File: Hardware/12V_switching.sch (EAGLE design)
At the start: 10 parts, among them IC5 LM2576D2TR4-5G, J1 POWERPOLE_POWER45A, J2 POWERPOLE_POWER45A

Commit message: Fix switching regulator reference
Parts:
- IC5: value LM2576D2TR4-5G -> LM2576D2TR4-012G; device LM2576D2TR4-5G:LM2576D2TR4-5G -> LM2576:LM2576D2TR4-012G
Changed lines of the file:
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@@
 </classes>
 <parts>
-<part name="IC5" library="LM2576D2TR4-5G" deviceset="LM2576D2TR4-5G" device=""/>
+<part name="IC5" library="LM2576" deviceset="LM2576D2TR4-012G" device=""/>
 <part name="GND12" library="supply1" deviceset="GND" device=""/>
 <part name="D2" library="diode" deviceset="DIODE-" device="DO-214AC" value="SAC32"/>

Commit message: Fix dimention layer on  RTI-Dome-eth.brd, added MPN on all component for mouser.
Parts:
- removed X11: (no value), con-ptr500:AK500/2
- added J3: POWERPOLE_POWER45A, powerpoles:POWERPOLE_POWER45A
- U$1: device rti:C-EU'1206' -> rti:C-EU'0805'
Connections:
- net +VIN: no longer X11-1.KL
- net GND: no longer X11-2.KL
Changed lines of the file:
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@@
 <part name="C10" library="rcl" deviceset="CPOL-EU" device="UD-10X10" value="100uF"/>
 <part name="C11" library="rcl" deviceset="CPOL-EU" device="UD-10X10" value="1000uF"/>
-<part name="U$1" library="rti" deviceset="C-EU" device="'1206'" value="47uF"/>
+<part name="U$1" library="rti" deviceset="C-EU" device="'0805'" value="47uF"/>
 <part name="U$2" library="rti" deviceset="C-EU" device="'1206'" value="47uF"/>
 <part name="J1" library="powerpoles" deviceset="POWERPOLE_POWER" device="45A"/>
 <part name="J2" library="powerpoles" deviceset="POWERPOLE_POWER" device="45A"/>
-<part name="X11" library="con-ptr500" deviceset="AK500/2" device=""/>
+<part name="J3" library="powerpoles" deviceset="POWERPOLE_POWER" device="45A"/>
 </parts>
 <sheets>
@@
 <instance part="J1" gate="G$1" x="10.16" y="48.26" rot="R180"/>
 <instance part="J2" gate="G$1" x="157.48" y="30.48"/>
-<instance part="X11" gate="-1" x="15.24" y="12.7"/>
-<instance part="X11" gate="-2" x="15.24" y="7.62"/>
+<instance part="J3" gate="G$1" x="172.72" y="5.08"/>
 </instances>
 <busses>
@@
 </segment>
 <segment>
-<wire x1="22.86" y1="7.62" x2="20.32" y2="7.62" width="0.1524" layer="91"/>
-<label x="22.86" y="7.62" size="1.016" layer="95" rot="MR180" xref="yes"/>
-<pinref part="X11" gate="-2" pin="KL"/>
+<wire x1="160.02" y1="0" x2="162.56" y2="0" width="0.1524" layer="91"/>
+<label x="160.02" y="0" size="1.016" layer="95" rot="MR0" xref="yes"/>
 </segment>
 </net>
@@
 </segment>
 <segment>
-<wire x1="22.86" y1="12.7" x2="20.32" y2="12.7" width="0.1524" layer="91"/>
-<label x="22.86" y="12.7" size="1.016" layer="95" rot="MR180" xref="yes"/>
-<pinref part="X11" gate="-1" pin="KL"/>
+<wire x1="160.02" y1="10.16" x2="162.56" y2="10.16" width="0.1524" layer="91"/>
+<label x="160.02" y="10.16" size="1.016" layer="95" rot="MR0" xref="yes"/>
 </segment>
 </net>

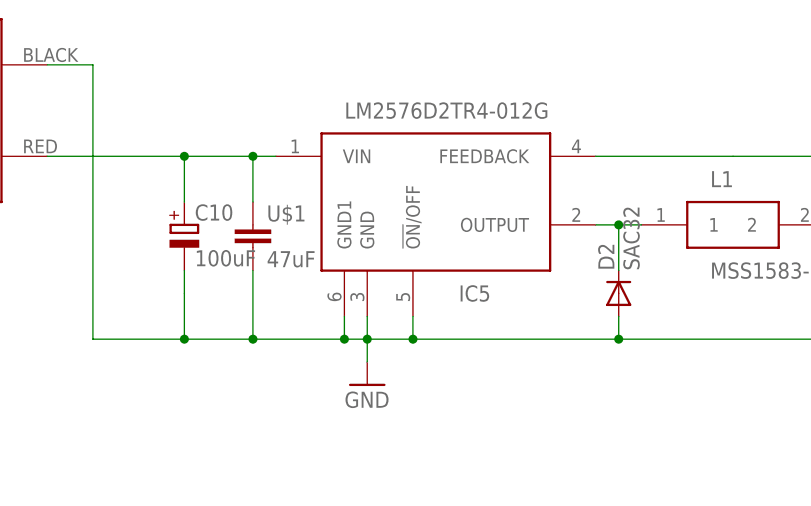
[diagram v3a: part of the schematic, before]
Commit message: Change pin mode for better interrupt detection
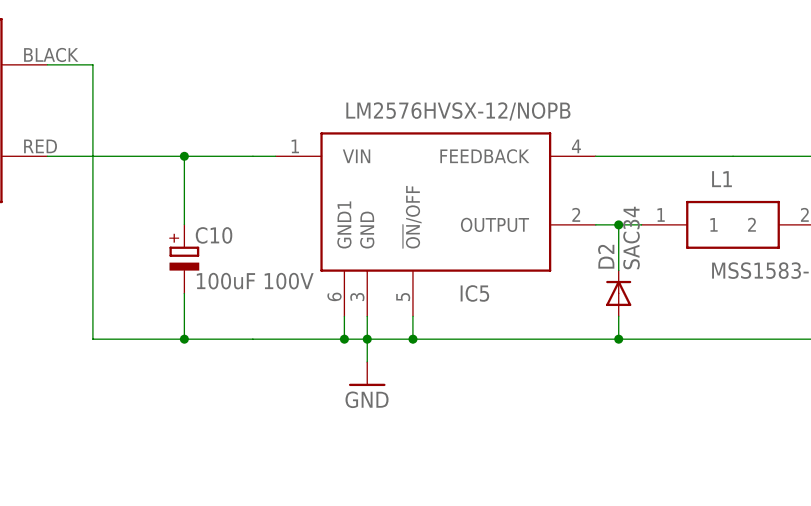
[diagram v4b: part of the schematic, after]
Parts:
- removed U$1: 47uF, rti:C-EU'0805'
- C10: value 100uF -> 100uF 100V
- D2: value SAC32 -> SAC34
- IC5: value LM2576D2TR4-012G -> LM2576HVSX-12/NOPB; MOUSER_PART_NUMBER (none) -> LM2576HVSX-12/NOPB; MPN (none) -> LM2576HVSX-12/NOPB
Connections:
- net +VIN: no longer U$1.1
- net GND: no longer U$1.2
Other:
- moved on the sheet: C10
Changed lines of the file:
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@@
 </classes>
 <parts>
-<part name="IC5" library="LM2576" deviceset="LM2576D2TR4-012G" device=""/>
+<part name="IC5" library="LM2576" deviceset="LM2576D2TR4-012G" device="" value="LM2576HVSX-12/NOPB">
+<attribute name="MOUSER_PART_NUMBER" value=" LM2576HVSX-12/NOPB"/>
+<attribute name="MPN" value=" LM2576HVSX-12/NOPB"/>
+</part>
 <part name="GND12" library="supply1" deviceset="GND" device=""/>
-<part name="D2" library="diode" deviceset="DIODE-" device="DO-214AC" value="SAC32"/>
+<part name="D2" library="diode" deviceset="DIODE-" device="DO-214AC" value="SAC34"/>
 <part name="L1" library="MSS1583-104KEB" deviceset="MSS1583-104KEB" device=""/>
-<part name="C10" library="rcl" deviceset="CPOL-EU" device="UD-10X10" value="100uF"/>
+<part name="C10" library="rcl" deviceset="CPOL-EU" device="UD-10X10" value="100uF 100V"/>
 <part name="C11" library="rcl" deviceset="CPOL-EU" device="UD-10X10" value="1000uF"/>
-<part name="U$1" library="rti" deviceset="C-EU" device="'0805'" value="47uF"/>
 <part name="U$2" library="rti" deviceset="C-EU" device="'1206'" value="47uF"/>
 <part name="J1" library="powerpoles" deviceset="POWERPOLE_POWER" device="45A"/>
@@
 <instance part="D2" gate="G$1" x="83.82" y="27.94" rot="R90"/>
 <instance part="L1" gate="G$1" x="96.52" y="35.56"/>
-<instance part="C10" gate="G$1" x="35.56" y="35.56"/>
+<instance part="C10" gate="G$1" x="35.56" y="33.02"/>
 <instance part="C11" gate="G$1" x="114.3" y="30.48"/>
-<instance part="U$1" gate="G$1" x="43.18" y="35.56"/>
 <instance part="U$2" gate="G$1" x="124.46" y="30.48"/>
 <instance part="J1" gate="G$1" x="10.16" y="48.26" rot="R180"/>
@@
 <wire x1="43.18" y1="22.86" x2="35.56" y2="22.86" width="0.1524" layer="91"/>
 <wire x1="35.56" y1="22.86" x2="35.56" y2="27.94" width="0.1524" layer="91"/>
-<wire x1="35.56" y1="27.94" x2="35.56" y2="30.48" width="0.1524" layer="91"/>
 <wire x1="60.96" y1="22.86" x2="83.82" y2="22.86" width="0.1524" layer="91"/>
 <junction x="60.96" y="22.86"/>
@@
 <junction x="114.3" y="22.86"/>
 <wire x1="124.46" y1="22.86" x2="137.16" y2="22.86" width="0.1524" layer="91"/>
-<pinref part="U$1" gate="G$1" pin="2"/>
-<wire x1="43.18" y1="30.48" x2="43.18" y2="22.86" width="0.1524" layer="91"/>
-<junction x="43.18" y="22.86"/>
 <pinref part="U$2" gate="G$1" pin="2"/>
 <wire x1="124.46" y1="25.4" x2="124.46" y2="22.86" width="0.1524" layer="91"/>
@@
 <wire x1="35.56" y1="43.18" x2="43.18" y2="43.18" width="0.1524" layer="91"/>
 <wire x1="43.18" y1="43.18" x2="45.72" y2="43.18" width="0.1524" layer="91"/>
-<wire x1="35.56" y1="43.18" x2="35.56" y2="38.1" width="0.1524" layer="91"/>
+<wire x1="35.56" y1="43.18" x2="35.56" y2="35.56" width="0.1524" layer="91"/>
 <junction x="35.56" y="43.18"/>
-<pinref part="U$1" gate="G$1" pin="1"/>
-<wire x1="43.18" y1="43.18" x2="43.18" y2="38.1" width="0.1524" layer="91"/>
-<junction x="43.18" y="43.18"/>
 <pinref part="J1" gate="G$1" pin="V+"/>
 </segment>

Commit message: Fix a non connected network on the board... the motor VOut .. :(
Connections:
- net +VIN: now also J3.V+
- net GND: now also J3.GND
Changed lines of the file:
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@@
 <wire x1="160.02" y1="0" x2="162.56" y2="0" width="0.1524" layer="91"/>
 <label x="160.02" y="0" size="1.016" layer="95" rot="MR0" xref="yes"/>
+<pinref part="J3" gate="G$1" pin="GND"/>
 </segment>
 </net>
@@
 <wire x1="160.02" y1="10.16" x2="162.56" y2="10.16" width="0.1524" layer="91"/>
 <label x="160.02" y="10.16" size="1.016" layer="95" rot="MR0" xref="yes"/>
+<pinref part="J3" gate="G$1" pin="V+"/>
 </segment>
 </net>

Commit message: Update some of the components on the 12V adapter.
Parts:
- C10, C11: device rcl:CPOL-EUUD-10X10 -> rti:CPOL-EU
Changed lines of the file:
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@@
 <part name="D2" library="diode" deviceset="DIODE-" device="DO-214AC" value="SAC34"/>
 <part name="L1" library="MSS1583-104KEB" deviceset="MSS1583-104KEB" device=""/>
-<part name="C10" library="rcl" deviceset="CPOL-EU" device="UD-10X10" value="100uF 100V"/>
-<part name="C11" library="rcl" deviceset="CPOL-EU" device="UD-10X10" value="1000uF"/>
+<part name="C10" library="rti" deviceset="CPOL-EU" device="" value="100uF 100V"/>
+<part name="C11" library="rti" deviceset="CPOL-EU" device="" value="1000uF"/>
 <part name="U$2" library="rti" deviceset="C-EU" device="'1206'" value="47uF"/>
 <part name="J1" library="powerpoles" deviceset="POWERPOLE_POWER" device="45A"/>
@@
 <instance part="J1" gate="G$1" x="10.16" y="48.26" rot="R180"/>
 <instance part="J2" gate="G$1" x="157.48" y="30.48"/>
-<instance part="J3" gate="G$1" x="172.72" y="5.08"/>
+<instance part="J3" gate="G$1" x="157.48" y="5.08"/>
 </instances>
 <busses>
@@
 </segment>
 <segment>
-<wire x1="160.02" y1="0" x2="162.56" y2="0" width="0.1524" layer="91"/>
-<label x="160.02" y="0" size="1.016" layer="95" rot="MR0" xref="yes"/>
+<wire x1="144.78" y1="0" x2="147.32" y2="0" width="0.1524" layer="91"/>
+<label x="144.78" y="0" size="1.016" layer="95" rot="MR0" xref="yes"/>
 <pinref part="J3" gate="G$1" pin="GND"/>
 </segment>
@@
 </segment>
 <segment>
-<wire x1="160.02" y1="10.16" x2="162.56" y2="10.16" width="0.1524" layer="91"/>
-<label x="160.02" y="10.16" size="1.016" layer="95" rot="MR0" xref="yes"/>
+<wire x1="144.78" y1="10.16" x2="147.32" y2="10.16" width="0.1524" layer="91"/>
+<label x="144.78" y="10.16" size="1.016" layer="95" rot="MR0" xref="yes"/>
 <pinref part="J3" gate="G$1" pin="V+"/>
 </segment>

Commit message: Fix merge conflict
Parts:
- C10, C11: device rti:CPOL-EU -> rcl:CPOL-EUUD-10X10
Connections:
- net +VIN: no longer J3.V+
- net GND: no longer J3.GND
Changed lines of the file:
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@@
 <part name="D2" library="diode" deviceset="DIODE-" device="DO-214AC" value="SAC34"/>
 <part name="L1" library="MSS1583-104KEB" deviceset="MSS1583-104KEB" device=""/>
-<part name="C10" library="rti" deviceset="CPOL-EU" device="" value="100uF 100V"/>
-<part name="C11" library="rti" deviceset="CPOL-EU" device="" value="1000uF"/>
+<part name="C10" library="rcl" deviceset="CPOL-EU" device="UD-10X10" value="100uF 100V"/>
+<part name="C11" library="rcl" deviceset="CPOL-EU" device="UD-10X10" value="1000uF"/>
 <part name="U$2" library="rti" deviceset="C-EU" device="'1206'" value="47uF"/>
 <part name="J1" library="powerpoles" deviceset="POWERPOLE_POWER" device="45A"/>
@@
 <instance part="J1" gate="G$1" x="10.16" y="48.26" rot="R180"/>
 <instance part="J2" gate="G$1" x="157.48" y="30.48"/>
-<instance part="J3" gate="G$1" x="157.48" y="5.08"/>
+<instance part="J3" gate="G$1" x="172.72" y="5.08"/>
 </instances>
 <busses>
@@
 </segment>
 <segment>
-<wire x1="144.78" y1="0" x2="147.32" y2="0" width="0.1524" layer="91"/>
-<label x="144.78" y="0" size="1.016" layer="95" rot="MR0" xref="yes"/>
-<pinref part="J3" gate="G$1" pin="GND"/>
+<wire x1="160.02" y1="0" x2="162.56" y2="0" width="0.1524" layer="91"/>
+<label x="160.02" y="0" size="1.016" layer="95" rot="MR0" xref="yes"/>
 </segment>
 </net>
@@
 </segment>
 <segment>
-<wire x1="144.78" y1="10.16" x2="147.32" y2="10.16" width="0.1524" layer="91"/>
-<label x="144.78" y="10.16" size="1.016" layer="95" rot="MR0" xref="yes"/>
-<pinref part="J3" gate="G$1" pin="V+"/>
+<wire x1="160.02" y1="10.16" x2="162.56" y2="10.16" width="0.1524" layer="91"/>
+<label x="160.02" y="10.16" size="1.016" layer="95" rot="MR0" xref="yes"/>
 </segment>
 </net>
